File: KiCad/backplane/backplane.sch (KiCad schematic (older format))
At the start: 18 parts, among them J1 Barrel_Jack_Switch, J2 USB_C_Receptacle, Q1 AOD403, Q2 AOD403, SW1 POWER

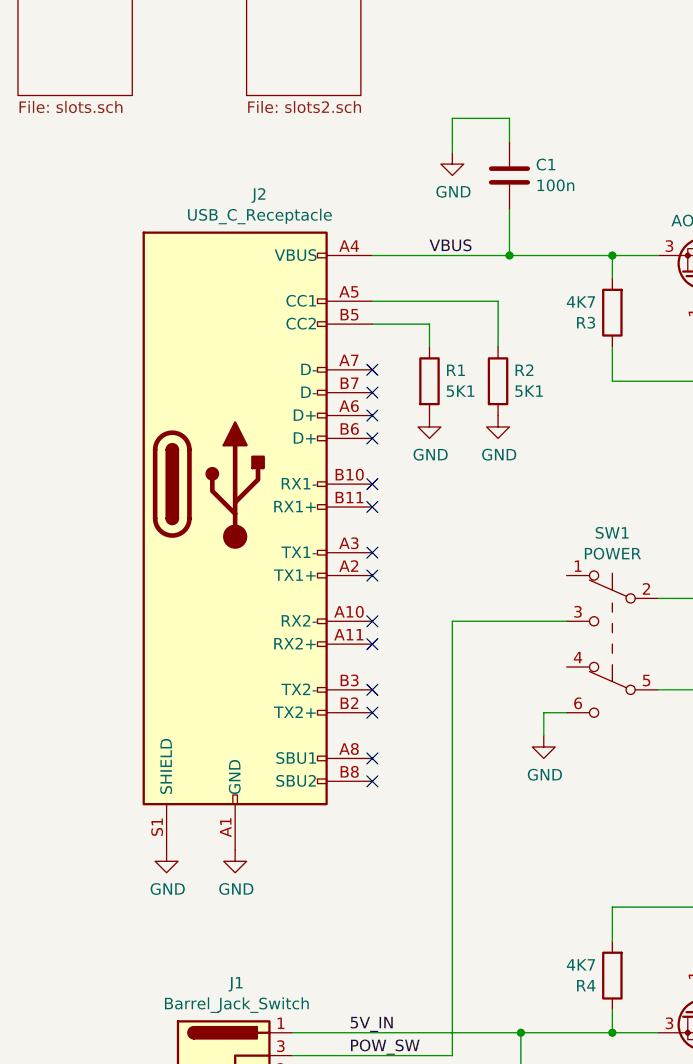
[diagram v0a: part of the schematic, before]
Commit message: Changed USB C receptable
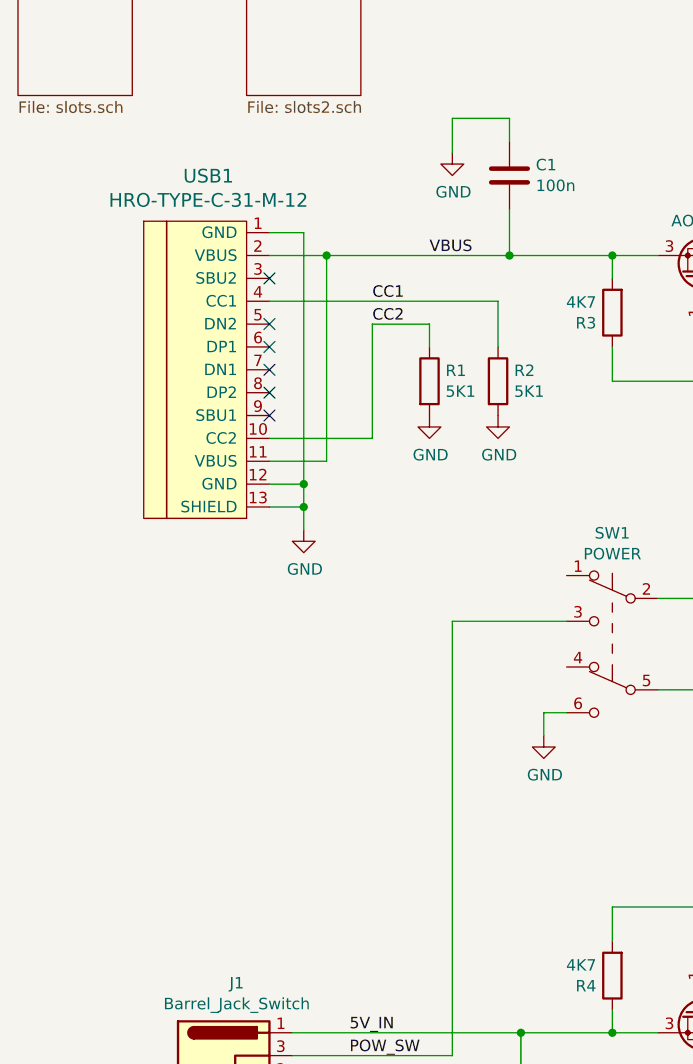
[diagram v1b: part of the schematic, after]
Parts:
- removed J2: USB_C_Receptacle, Connector_USB:USB_C_Receptacle_Amphenol_12401548E4-2A, symbol Connector:USB_C_Receptacle
- added USB1: HRO-TYPE-C-31-M-12, Mini8086:HRO-TYPE-C-31-M-12, symbol Type-C:HRO-TYPE-C-31-M-12
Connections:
- net GND: now also USB1.1 (GND), USB1.12 (GND), USB1.13 (SHIELD)
- net VBUS: now also USB1.11 (VBUS), USB1.2 (VBUS)
- net CC1: now reaches R2.1
- net CC1: now also USB1.4 (CC1)
- net CC2: now reaches R1.1
- net CC2: now also USB1.10 (CC2)
- no-connect marks 14 -> 6
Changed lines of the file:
@@
 $EndDescr
-$Comp
-L Connector:USB_C_Receptacle J2
-U 1 1 5FFE7DD5
-P 1950 3200
-F 0 "J2" H 2057 4467 50  0000 C CNN
-F 1 "USB_C_Receptacle" H 2057 4376 50  0000 C CNN
-F 2 "Connector_USB:USB_C_Receptacle_Amphenol_12401548E4-2A" H 2100 3200 50  0001 C CNN
-F 3 "https://www.usb.org/sites/default/files/documents/usb_type-c.zip" H 2100 3200 50  0001 C CNN
-	1    1950 3200
-	1    0    0    -1
-$EndComp
 $Comp
 L Connector:Barrel_Jack_Switch J1
@@
 	1    0    0    -1
 $EndComp
-NoConn ~ 2550 4500
-NoConn ~ 2550 4400
-NoConn ~ 2550 4200
-NoConn ~ 2550 4100
-NoConn ~ 2550 3900
-NoConn ~ 2550 3800
-NoConn ~ 2550 3600
-NoConn ~ 2550 3500
-NoConn ~ 2550 3300
-NoConn ~ 2550 3200
-NoConn ~ 2550 3000
-NoConn ~ 2550 2900
-NoConn ~ 2550 2800
-NoConn ~ 2550 2700
 $Comp
 L power:GND #PWR02
 U 1 1 5FFEB95A
-P 1950 4800
-F 0 "#PWR02" H 1950 4550 50  0001 C CNN
-F 1 "GND" H 1955 4627 50  0000 C CNN
-F 2 "" H 1950 4800 50  0001 C CNN
-F 3 "" H 1950 4800 50  0001 C CNN
-	1    1950 4800
-	1    0    0    -1
-$EndComp
-$Comp
-L power:GND #PWR01
-U 1 1 5FFEBD3F
-P 1650 4800
-F 0 "#PWR01" H 1650 4550 50  0001 C CNN
-F 1 "GND" H 1655 4627 50  0000 C CNN
-F 2 "" H 1650 4800 50  0001 C CNN
-F 3 "" H 1650 4800 50  0001 C CNN
-	1    1650 4800
+P 2250 3400
+F 0 "#PWR02" H 2250 3150 50  0001 C CNN
+F 1 "GND" H 2255 3227 50  0000 C CNN
+F 2 "" H 2250 3400 50  0001 C CNN
+F 3 "" H 2250 3400 50  0001 C CNN
+	1    2250 3400
 	1    0    0    -1
 $EndComp
@@
 Wire Wire Line
 	2800 2500 2800 2600
-Wire Wire Line
-	2550 2400 3100 2400
 Wire Wire Line
 	3100 2400 3100 2600
@@
 	-1   0    0    1
 $EndComp
-Wire Wire Line
-	2550 2200 3150 2200
 Text Label 2800 2200 0    50   ~ 0
 VBUS
@@
 	0    1    1    0
 $EndComp
+$Comp
+L Type-C:HRO-TYPE-C-31-M-12 USB1
+U 1 1 601914F2
+P 2000 2650
+F 0 "USB1" H 1833 3447 60  0000 C CNN
+F 1 "HRO-TYPE-C-31-M-12" H 1833 3341 60  0000 C CNN
+F 2 "Mini8086:HRO-TYPE-C-31-M-12" H 2000 2650 60  0001 C CNN
+F 3 "" H 2000 2650 60  0001 C CNN
+	1    2000 2650
+	1    0    0    -1
+$EndComp
+Wire Wire Line
+	2100 3000 2550 3000
+Wire Wire Line
+	2550 3000 2550 2500
+Wire Wire Line
+	2100 3100 2350 3100
+Wire Wire Line
+	2250 3400 2250 3300
+Wire Wire Line
+	2250 3300 2100 3300
+Wire Wire Line
+	2100 3200 2250 3200
+Wire Wire Line
+	2250 3200 2250 3300
+Connection ~ 2250 3300
+Wire Wire Line
+	2250 3200 2250 2100
+Wire Wire Line
+	2250 2100 2100 2100
+Connection ~ 2250 3200
+NoConn ~ 2100 2900
+NoConn ~ 2100 2800
+NoConn ~ 2100 2700
+NoConn ~ 2100 2600
+NoConn ~ 2100 2500
+NoConn ~ 2100 2300
+Wire Wire Line
+	2100 2400 3100 2400
+Wire Wire Line
+	2350 3100 2350 2200
+Wire Wire Line
+	2100 2200 2350 2200
+Connection ~ 2350 2200
+Wire Wire Line
+	2350 2200 3150 2200
+Text Label 2550 2400 0    50   ~ 0
+CC1
+Text Label 2550 2500 0    50   ~ 0
+CC2
 $EndSCHEMATC

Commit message: Fixed backplaneV2 bugs
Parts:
- USB1: symbol Type-C:HRO-TYPE-C-31-M-12 -> backplane-rescue:HRO-TYPE-C-31-M-12-Type-C
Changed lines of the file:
@@
 	2200 5600 3200 5600
 Wire Wire Line
-	4800 2200 4800 5600
+	4500 2200 4500 5600
 Wire Wire Line
 	5700 2200 5250 2200
 Connection ~ 5700 2200
-Connection ~ 4800 2200
+Connection ~ 4500 2200
 Wire Wire Line
 	7050 2400 7050 2200
@@
 Connection ~ 5250 2200
 Wire Wire Line
-	5250 2200 4800 2200
-Wire Wire Line
-	4200 2200 4800 2200
-Wire Wire Line
-	4200 5600 4800 5600
+	5250 2200 4500 2200
+Wire Wire Line
+	4200 2200 4500 2200
+Wire Wire Line
+	4200 5600 4500 5600
 $Comp
 L Transistor_FET:QM6015D Q1
@@
 $EndComp
 $Comp
-L Type-C:HRO-TYPE-C-31-M-12 USB1
+L backplane-rescue:HRO-TYPE-C-31-M-12-Type-C USB1
 U 1 1 601914F2
 P 2000 2650
